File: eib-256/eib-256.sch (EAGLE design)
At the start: 68 parts

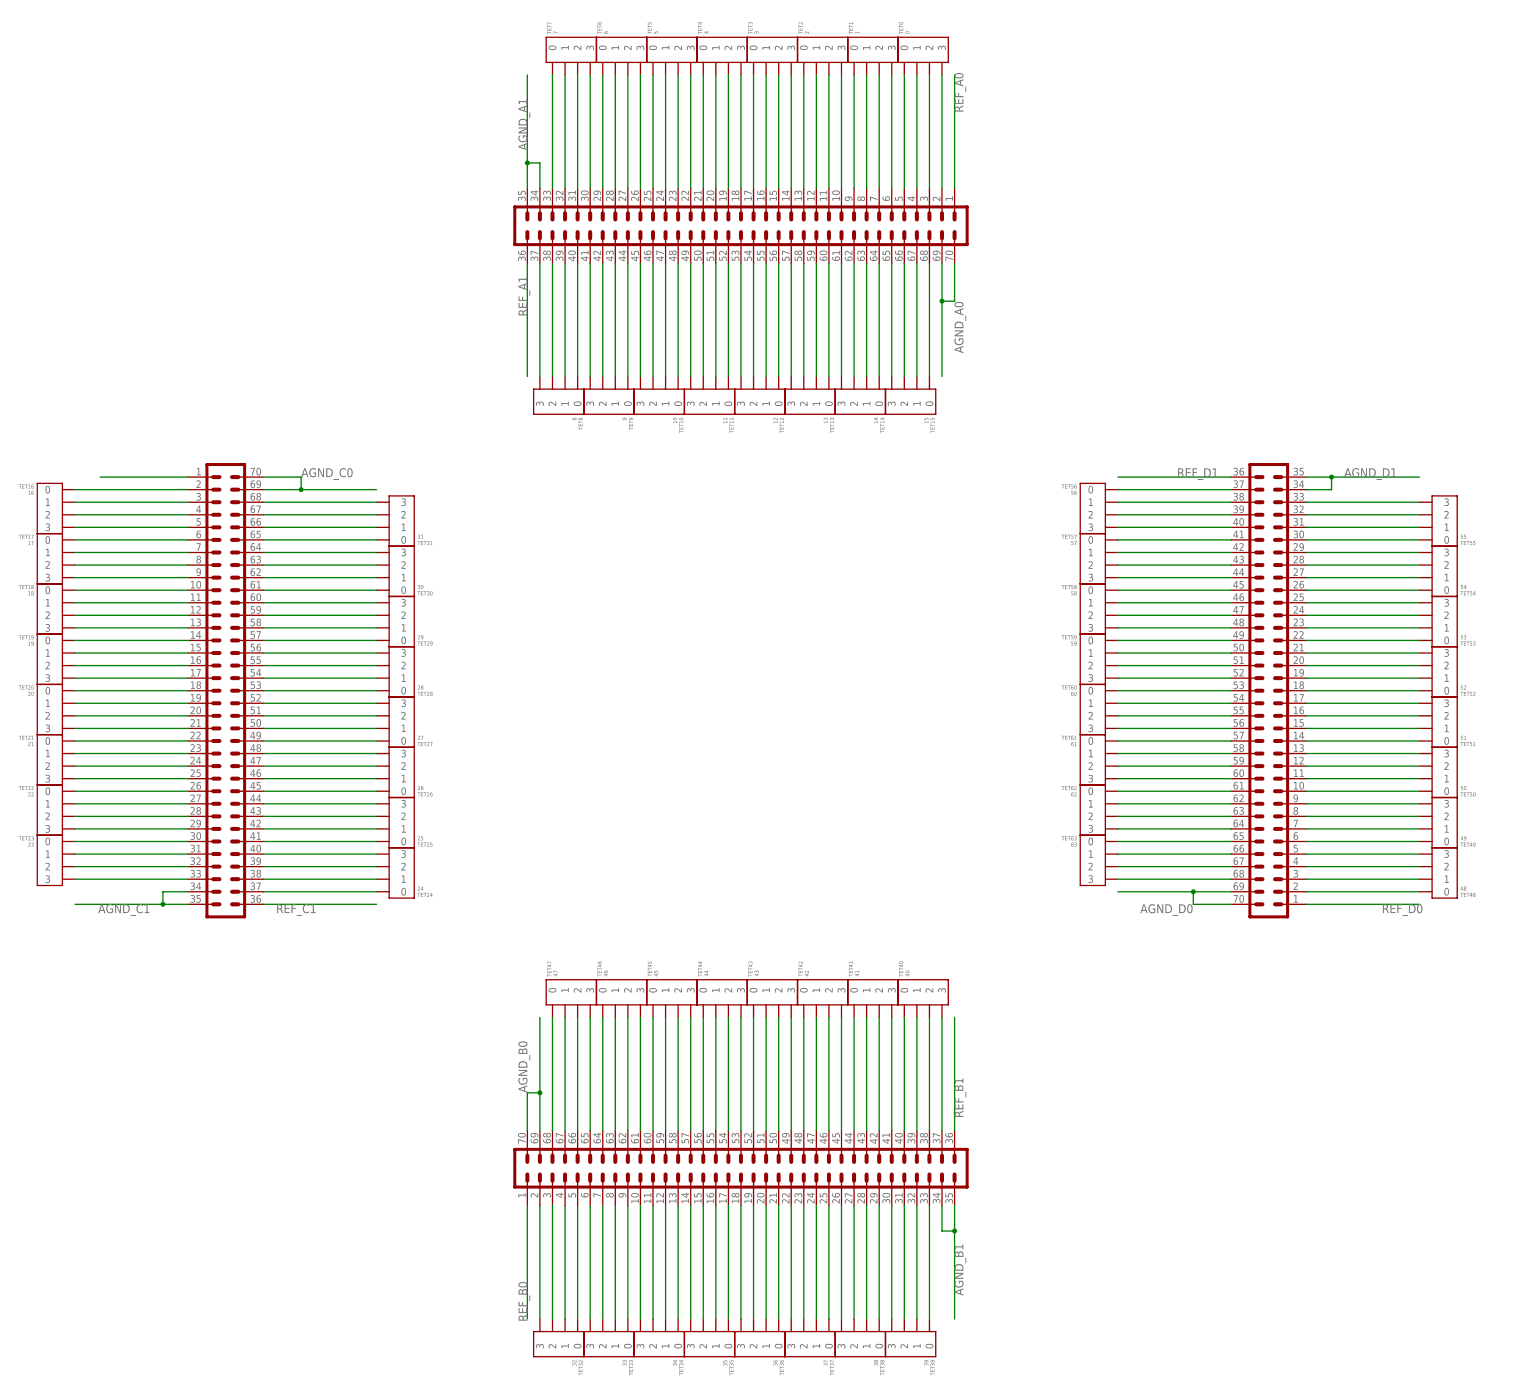
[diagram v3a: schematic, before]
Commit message: Complete 256 channel EIB
- Sent out for an assembly quotation at PCBCart. Before proceeding, I
  need to have a good look over the board.
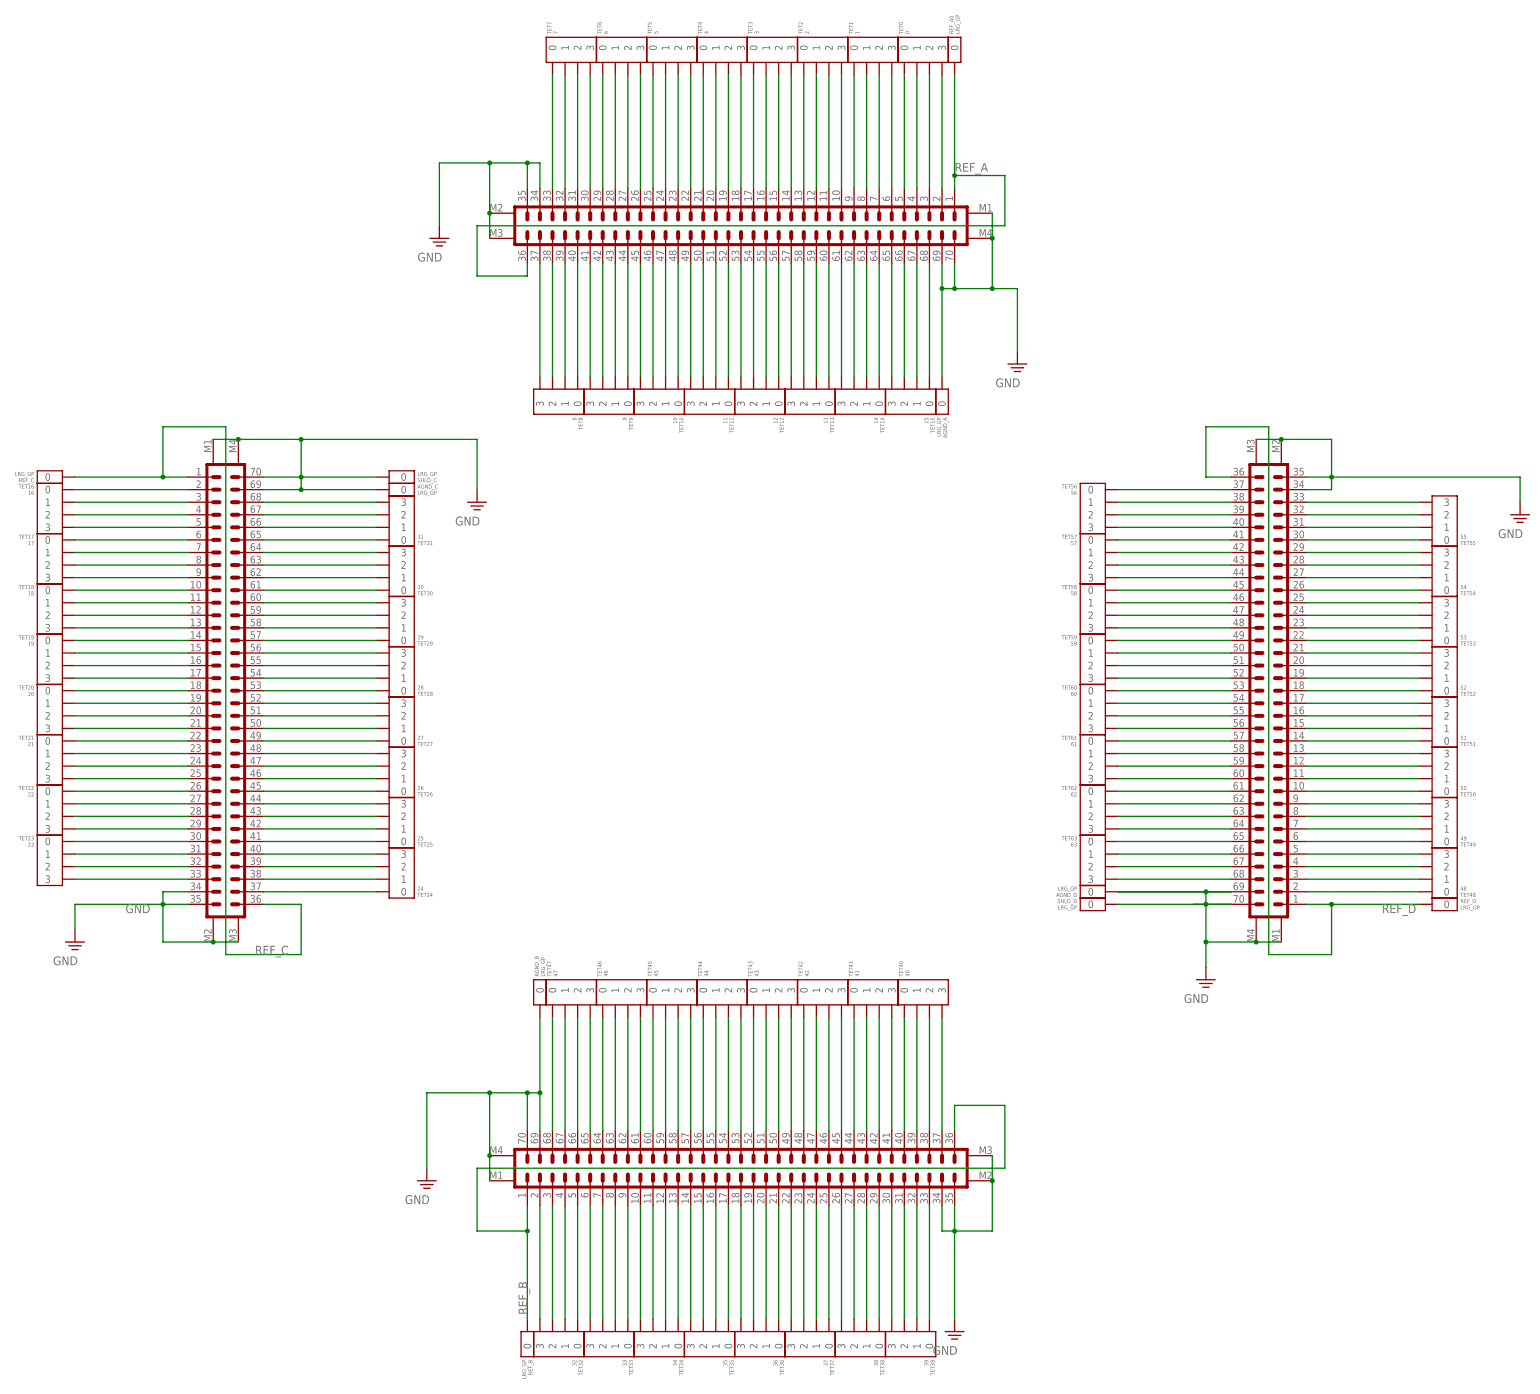
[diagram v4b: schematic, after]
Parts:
- added AGND_A, AGND_B, AGND_C, AGND_D, REF_A0, REF_B, REF_C, REF_D, SHLD_C, SHLD_D: LRG_GP, jonnew:GOLDPIN_0.5ID_0.7OD
- A, B, C, D: device jonnew:PINHD-2X35_DF40HEAD -> jonnew:PINHD-2X35+4_DF40-70HEAD
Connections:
- removed net AGND_A0: A.69, A.70
- removed net AGND_A1: A.34, A.35
- removed net AGND_B0: B.69, B.70
- removed net AGND_B1: B.34, B.35
- removed net AGND_C0: C.69, C.70
- removed net AGND_C1: C.34, C.35
- removed net AGND_D1: D.34, D.35
- removed net REF_A0: A.1
- removed net REF_A1: A.36
- removed net REF_B0: B.1
- removed net REF_B1: B.36
- removed net REF_C0: C.1
- removed net REF_C1: C.36
- removed net REF_D0: D.1
- removed net REF_D1: D.36
- new net GND: A.34, A.35, A.69, A.70, A.M1, A.M2, A.M3, A.M4, AGND_A.0, AGND_B.0, AGND_C.0, AGND_D.0, B.34, B.35, B.69, B.70, B.M1, B.M2, B.M3, B.M4, C.34, C.35, C.69, C.70, C.M1, C.M2, C.M3, C.M4, D.34, D.35, D.M1, D.M2, D.M3, D.M4, SHLD_C.0, SHLD_D.0
- new net N$97: D.70
- new net REF_A: A.1, A.36, REF_A0.0
- new net REF_B: B.1, B.36, REF_B.0
- new net REF_C: C.1, C.36, REF_C.0
- new net REF_D: D.1, D.36, REF_D.0
- net AGND_D0: no longer D.70

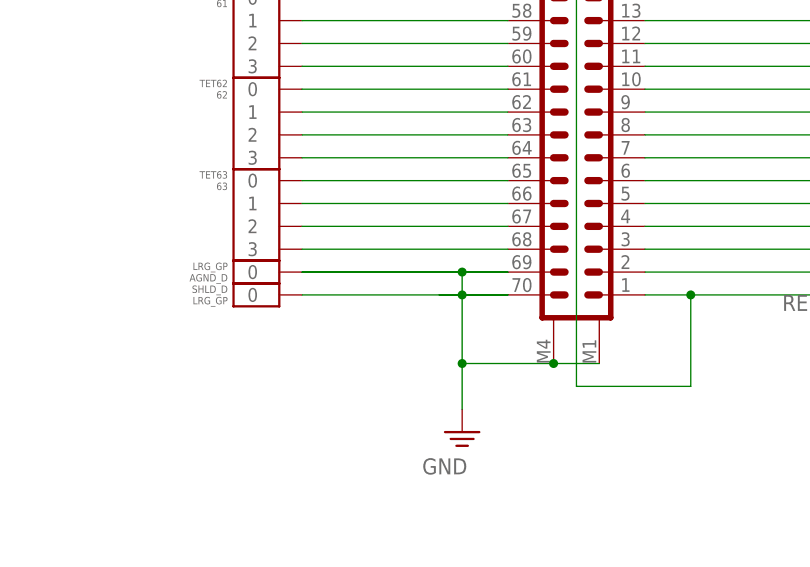
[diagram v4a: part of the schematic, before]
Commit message: Minor modifications to silkscreen of 256 channel EIB
- Also, a few more GND stiches added in/around DF40 connectors
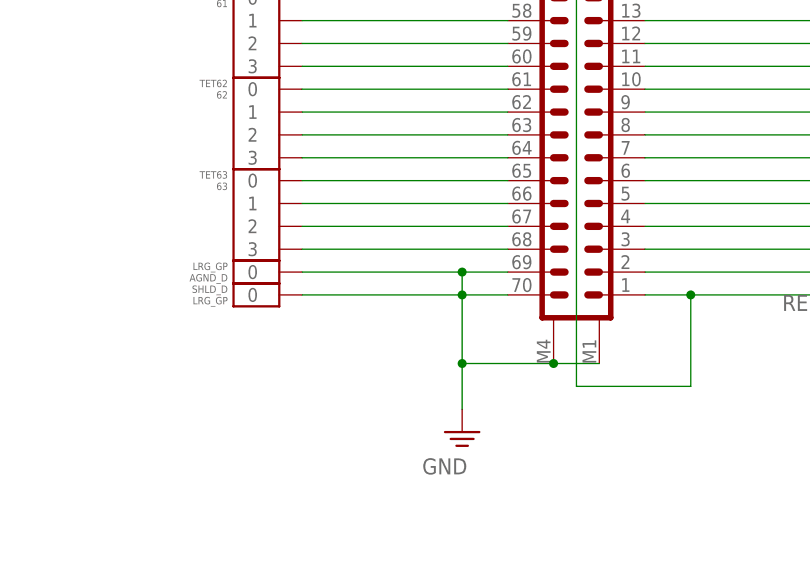
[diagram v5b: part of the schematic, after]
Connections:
- removed net AGND_D0: D.69
- removed net N$97: D.70
- net GND: now also D.69, D.70
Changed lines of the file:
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@@
-</segment>
-</net>
-<net name="AGND_D0" class="0">
-<segment>
-<wire x1="269.24" y1="116.84" x2="246.38" y2="116.84" width="0.1524" layer="91"/>
-<pinref part="D" gate="G$1" pin="69"/>
 </segment>
 </net>
@@
 <segment>
 <pinref part="SUPPLY3" gate="PE" pin="GND"/>
-<wire x1="269.24" y1="114.3" x2="264.16" y2="114.3" width="0.1524" layer="91"/>
-<wire x1="264.16" y1="114.3" x2="264.16" y2="116.84" width="0.1524" layer="91"/>
-<wire x1="264.16" y1="116.84" x2="269.24" y2="116.84" width="0.1524" layer="91"/>
-<wire x1="264.16" y1="116.84" x2="246.38" y2="116.84" width="0.1524" layer="91"/>
-<junction x="264.16" y="116.84"/>
-<pinref part="AGND_D" gate="G$1" pin="0"/>
 <pinref part="SHLD_D" gate="G$1" pin="0"/>
 <wire x1="264.16" y1="114.3" x2="246.38" y2="114.3" width="0.1524" layer="91"/>
@@
 <junction x="274.32" y="106.68"/>
 <junction x="264.16" y="106.68"/>
+<wire x1="264.16" y1="116.84" x2="246.38" y2="116.84" width="0.1524" layer="91"/>
+<wire x1="264.16" y1="114.3" x2="264.16" y2="116.84" width="0.1524" layer="91"/>
+<pinref part="D" gate="G$1" pin="69"/>
+<wire x1="264.16" y1="116.84" x2="269.24" y2="116.84" width="0.1524" layer="91"/>
+<junction x="264.16" y="116.84"/>
+<pinref part="D" gate="G$1" pin="70"/>
+<wire x1="264.16" y1="114.3" x2="269.24" y2="114.3" width="0.1524" layer="91"/>
+<pinref part="AGND_D" gate="G$1" pin="0"/>
 </segment>
 <segment>
@@
 </segment>
 </net>
-<net name="N$97" class="0">
-<segment>
-<pinref part="D" gate="G$1" pin="70"/>
-<wire x1="269.24" y1="114.3" x2="261.62" y2="114.3" width="0.1524" layer="91"/>
-</segment>
-</net>
